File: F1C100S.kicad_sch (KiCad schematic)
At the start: 45 parts, among them J1 Conn_02x04_Counter_Clockwise, J2 USB_B, Q1 Q_NMOS_GSD, SW1 SW_Push, U1 F1C100s, U2 JW5211, U3 JW5211, U4 JW5211, U5 AT25SF081-SSHD-X, Y1 24MHz

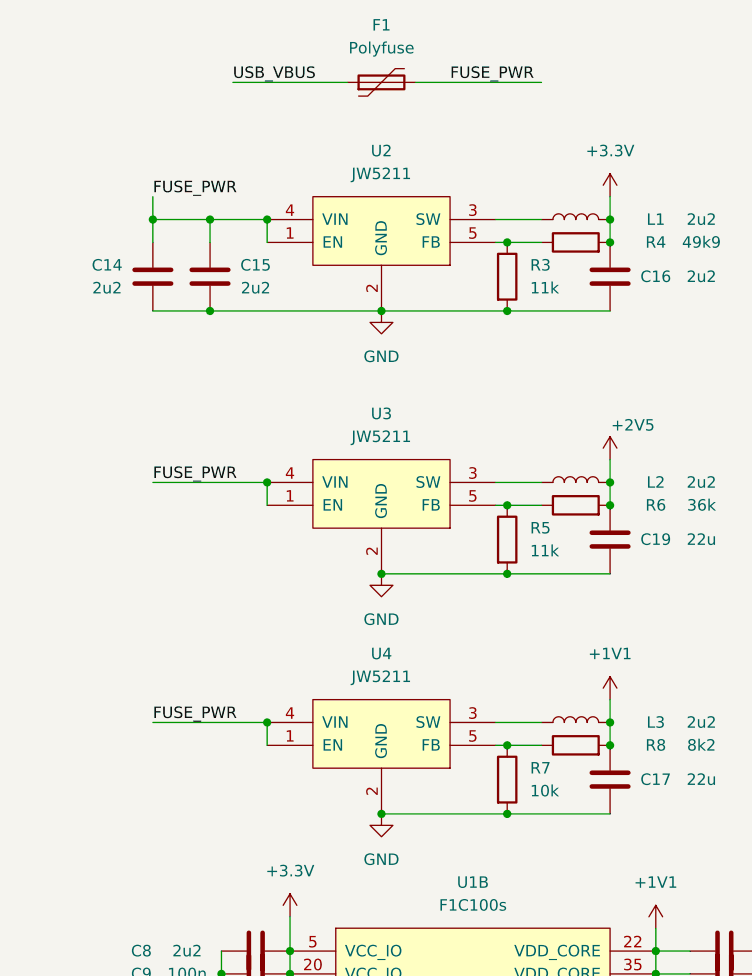
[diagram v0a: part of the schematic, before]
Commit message: feat: replace JW5211 to TLV62568DBV
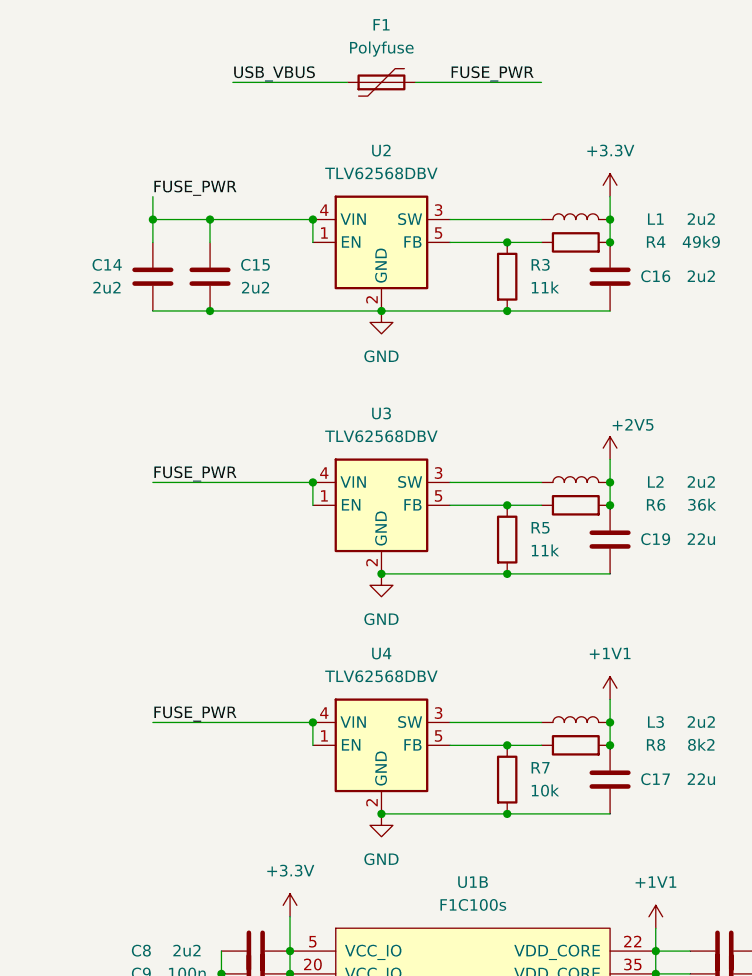
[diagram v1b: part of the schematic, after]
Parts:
- removed U2, U3, U4: JW5211, Package_TO_SOT_SMD:SOT-23-5, symbol 3340_kicad:JW5211
- added U2, U3, U4: TLV62568DBV, Package_TO_SOT_SMD:SOT-23-5, symbol Regulator_Switching:TLV62568DBV
- C1, C10, C11, C12, C13, C14, C15, C16, C17, C19, C2, C3, C4, C5, C6, C7, C8, C9: footprint (none) -> Capacitor_SMD:C_0603_1608Metric
- D1: footprint (none) -> LED_SMD:LED_0603_1608Metric
- L1, L2, L3: footprint (none) -> Inductor_SMD:L_0603_1608Metric
- R1, R10, R11, R12, R2, R3, R4, R5, R6, R7, R8, R9: footprint (none) -> Resistor_SMD:R_0603_1608Metric
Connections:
- net FUSE_PWR: now also U2.1 (EN), U2.4 (VIN), U3.1 (EN), U3.4 (VIN), U4.1 (EN), U4.4 (VIN)
- net GND: now also U2.2 (GND), U3.2 (GND), U4.2 (GND)
- net at R3.1, R4.1: now also U2.5 (FB)
- net at R7.1, R8.1: now also U4.5 (FB)
- net at L1.1: now also U2.3 (SW)
- net at L2.1: now also U3.3 (SW)
- net at R5.1, R6.1: now also U3.5 (FB)
- net at L3.1: now also U4.3 (SW)

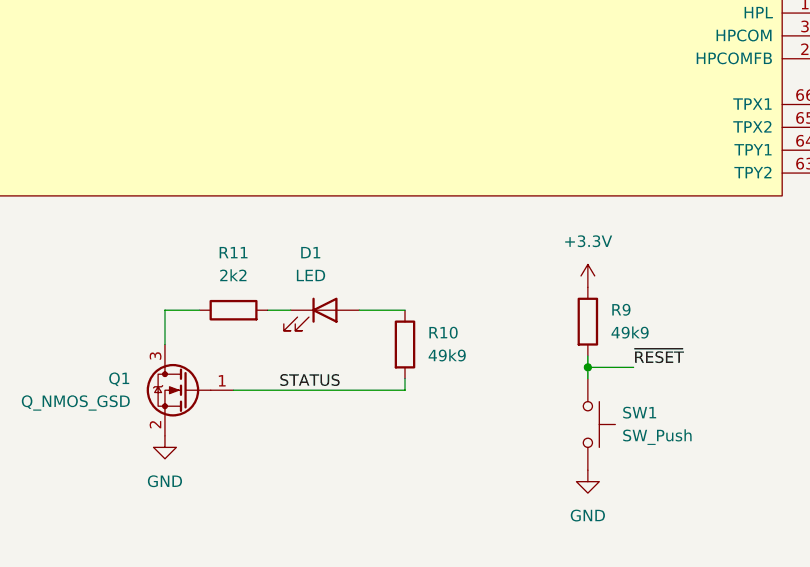
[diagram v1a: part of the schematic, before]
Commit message: fix: led 3v3
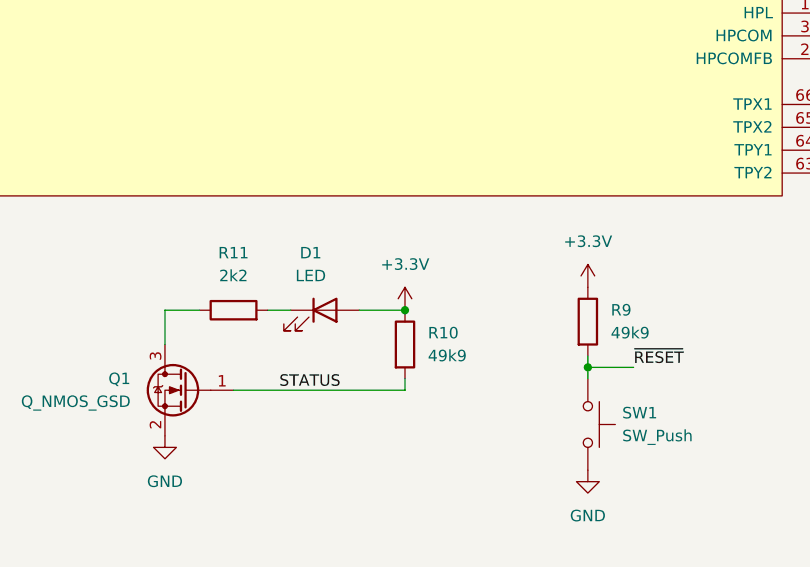
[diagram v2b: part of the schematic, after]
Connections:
- net +3.3V: now also D1.2 (A), R10.1
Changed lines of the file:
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@@
   (junction (at 105.41 146.05) (diameter 0) (color 0 0 0 0)
+  )
+  (junction (at 205.74 139.7) (diameter 0) (color 0 0 0 0)
   )
   (junction (at 40.64 39.37) (diameter 0) (color 0 0 0 0)
@@
         )
       )
+    )
+  )
+  (symbol (lib_id "power:+3.3V") (at 205.74 139.7 0) (unit 1)
+    (in_bom yes) (on_board yes) (dnp no) (fields_autoplaced)
+    (property "Reference" "#PWR030" (at 205.74 143.51 0)
+      (effects (font (size 1.27 1.27)) hide)
+    )
+    (property "Value" "+3.3V" (at 205.74 134.62 0)
+      (effects (font (size 1.27 1.27)))
+    )
+    (property "Footprint" "" (at 205.74 139.7 0)
+      (effects (font (size 1.27 1.27)) hide)
+    )
+    (property "Datasheet" "" (at 205.74 139.7 0)
+      (effects (font (size 1.27 1.27)) hide)
+    )
+    (pin "1")
+    (instances
+      (project "our_card"
+        (path "/efba4c66-4ab7-40a6-bb7c-80cfdf65f4a4/db197c2e-4b0a-442a-89c9-faca8b24731a"
+          (reference "#PWR030") (unit 1)
+        )
+      )

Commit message: feat: update footprint
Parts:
- F1: footprint (none) -> Resistor_SMD:R_0603_1608Metric_Pad0.98x0.95mm_HandSolder
- J1: footprint (none) -> Connector_PinHeader_2.54mm:PinHeader_2x04_P2.54mm_Vertical
- Q1: footprint (none) -> Package_TO_SOT_SMD:SOT-23-3
- SW1: footprint (none) -> Button_Switch_SMD:SW_SPST_TL3342
- Y1: footprint (none) -> Oscillator:Oscillator_SMD_Abracon_ASE-4Pin_3.2x2.5mm
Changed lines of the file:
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@@
       (effects (font (size 1.27 1.27)) (justify left))
     )
-    (property "Footprint" "" (at 176.53 146.05 0)
+    (property "Footprint" "Package_TO_SOT_SMD:SOT-23-3" (at 176.53 146.05 0)
       (effects (font (size 1.27 1.27)) hide)
     )
@@
       (effects (font (size 1.27 1.27)))
     )
-    (property "Footprint" "" (at 64.77 22.86 0)
+    (property "Footprint" "Resistor_SMD:R_0603_1608Metric_Pad0.98x0.95mm_HandSolder" (at 64.77 22.86 0)
       (effects (font (size 1.27 1.27)) (justify left) hide)
     )
@@
       (effects (font (size 1.27 1.27)))
     )
-    (property "Footprint" "" (at 35.56 179.07 0)
+    (property "Footprint" "Connector_PinHeader_2.54mm:PinHeader_2x04_P2.54mm_Vertical" (at 35.56 179.07 0)
       (effects (font (size 1.27 1.27)) hide)
     )
@@
       (effects (font (size 1.27 1.27)) (justify left))
     )
-    (property "Footprint" "" (at 231.14 152.4 0)
+    (property "Footprint" "Button_Switch_SMD:SW_SPST_TL3342" (at 231.14 152.4 0)
       (effects (font (size 1.27 1.27)) hide)
     )
@@
       (effects (font (size 1.27 1.27)))
     )
-    (property "Footprint" "" (at 266.7 27.94 0)
-      (effects (font (size 1.27 1.27)) hide)
-    )
+    (property "Footprint" "Oscillator:Oscillator_SMD_Abracon_ASE-4Pin_3.2x2.5mm" (at 266.7 27.94 0)
+      (effects (font (size 1.27 1.27)) hide)
+    )
